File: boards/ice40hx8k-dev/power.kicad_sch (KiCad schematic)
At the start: 22 parts, among them U1 ICE40HX8K-CT256

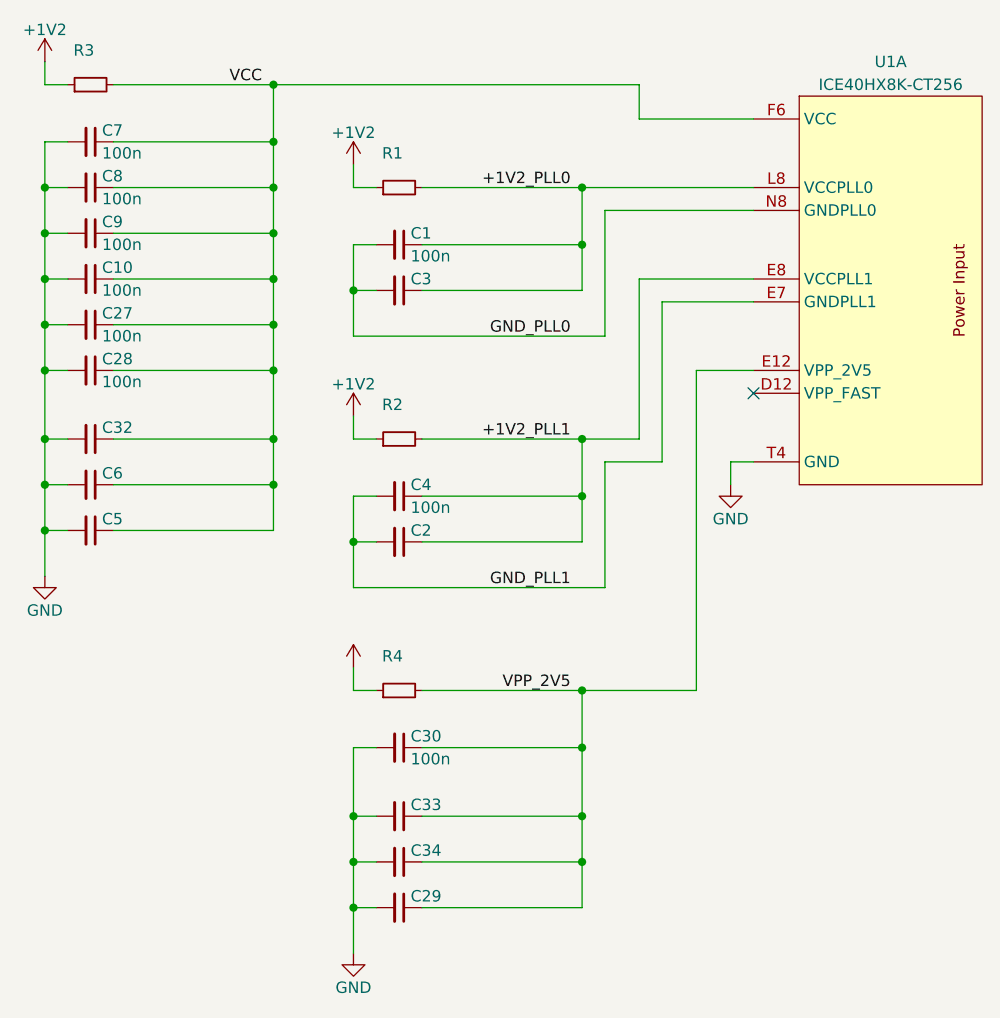
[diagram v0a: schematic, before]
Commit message: Switch to 6 layers, add power fills under BGA.
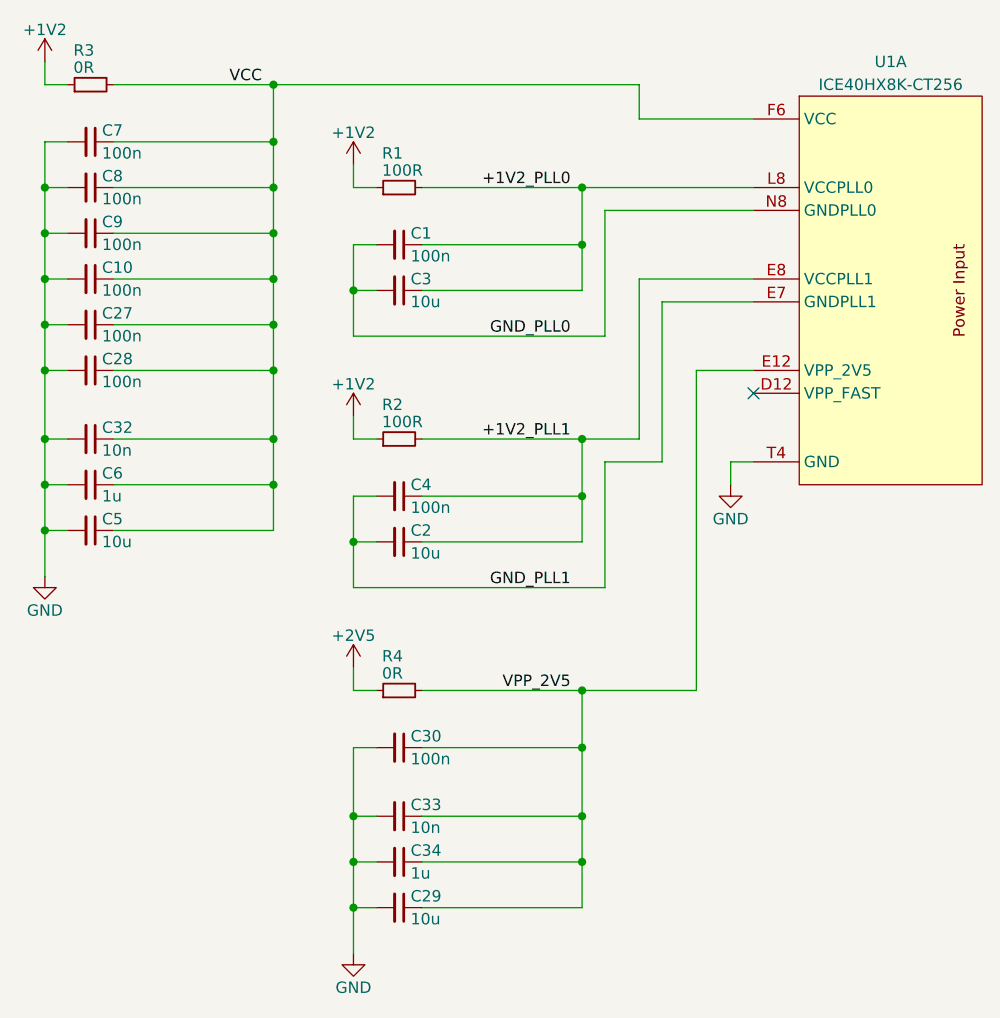
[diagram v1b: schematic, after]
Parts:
- C2, C29, C3, C5: value (none) -> 10u
- C32, C33: value (none) -> 10n
- C34, C6: value (none) -> 1u
- R1: value (none) -> 100R
- R2: value (none) -> 100R; footprint (none) -> 0Local:R_SMD_0402_Pad0.5mm
- R3: value (none) -> 0R
- R4: value (none) -> 0R; footprint (none) -> 0Local:R_SMD_0402_Pad0.5mm
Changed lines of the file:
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@@
       (effects (font (size 1.27 1.27)) (justify left))
     )
-    (property "Value" "" (id 1) (at 190.5 154.94 90)
+    (property "Value" "10u" (id 1) (at 190.5 154.94 90)
       (effects (font (size 1.27 1.27)) (justify left))
     )
@@
       (effects (font (size 1.27 1.27)) (justify right))
     )
-    (property "Value" "" (id 1) (at 153.035 60.325 90)
+    (property "Value" "0R" (id 1) (at 153.035 60.325 90)
       (effects (font (size 1.27 1.27)) (justify right))
     )
@@
       (effects (font (size 1.27 1.27)) (justify right))
     )
-    (property "Value" "" (id 1) (at 187.325 99.695 90)
-      (effects (font (size 1.27 1.27)) (justify right))
-    )
-    (property "Footprint" "" (id 2) (at 189.23 101.6 0)
+    (property "Value" "100R" (id 1) (at 187.325 99.695 90)
+      (effects (font (size 1.27 1.27)) (justify right))
+    )
+    (property "Footprint" "0Local:R_SMD_0402_Pad0.5mm" (id 2) (at 189.23 101.6 0)
       (effects (font (size 1.27 1.27)) hide)
     )
@@
       (effects (font (size 1.27 1.27)) hide)
     )
-    (property "Value" "" (id 1) (at 184.15 123.444 0))
+    (property "Value" "+2V5" (id 1) (at 184.15 123.444 0))
     (property "Footprint" "" (id 2) (at 184.15 127 0)
       (effects (font (size 1.27 1.27)) hide)
@@
       (effects (font (size 1.27 1.27)) (justify right))
     )
-    (property "Value" "" (id 1) (at 187.325 71.755 90)
+    (property "Value" "100R" (id 1) (at 187.325 71.755 90)
       (effects (font (size 1.27 1.27)) (justify right))
     )
@@
       (effects (font (size 1.27 1.27)) (justify right))
     )
-    (property "Value" "" (id 1) (at 187.325 127.635 90)
-      (effects (font (size 1.27 1.27)) (justify right))
-    )
-    (property "Footprint" "" (id 2) (at 189.23 129.54 0)
+    (property "Value" "0R" (id 1) (at 187.325 127.635 90)
+      (effects (font (size 1.27 1.27)) (justify right))
+    )
+    (property "Footprint" "0Local:R_SMD_0402_Pad0.5mm" (id 2) (at 189.23 129.54 0)
       (effects (font (size 1.27 1.27)) hide)
     )
@@
       (effects (font (size 1.27 1.27)) (justify left))
     )
-    (property "Value" "" (id 1) (at 156.21 113.03 90)
+    (property "Value" "10u" (id 1) (at 156.21 113.03 90)
       (effects (font (size 1.27 1.27)) (justify left))
     )
@@
       (effects (font (size 1.27 1.27)) (justify left))
     )
-    (property "Value" "" (id 1) (at 156.21 102.87 90)
+    (property "Value" "10n" (id 1) (at 156.21 102.87 90)
       (effects (font (size 1.27 1.27)) (justify left))
     )
@@
       (effects (font (size 1.27 1.27)) (justify left))
     )
-    (property "Value" "" (id 1) (at 190.5 144.78 90)
+    (property "Value" "10n" (id 1) (at 190.5 144.78 90)
       (effects (font (size 1.27 1.27)) (justify left))
     )
@@
       (effects (font (size 1.27 1.27)) (justify left))
     )
-    (property "Value" "" (id 1) (at 190.5 114.3 90)
+    (property "Value" "10u" (id 1) (at 190.5 114.3 90)
       (effects (font (size 1.27 1.27)) (justify left))
     )
@@
       (effects (font (size 1.27 1.27)) (justify left))
     )
-    (property "Value" "" (id 1) (at 156.21 107.95 90)
+    (property "Value" "1u" (id 1) (at 156.21 107.95 90)
       (effects (font (size 1.27 1.27)) (justify left))
     )
@@
       (effects (font (size 1.27 1.27)) (justify left))
     )
-    (property "Value" "" (id 1) (at 190.5 149.86 90)
+    (property "Value" "1u" (id 1) (at 190.5 149.86 90)
       (effects (font (size 1.27 1.27)) (justify left))
     )
@@
       (effects (font (size 1.27 1.27)) (justify left))
     )
-    (property "Value" "" (id 1) (at 190.5 86.36 90)
-      (effects (font (size 1.27 1.27)) (justify left))
-    )
+    (property "Value" "10u" (id 1) (at 190.5 86.36 90)
+      (effects (font (size 1.27 1.27)) (justify left))
+    )
